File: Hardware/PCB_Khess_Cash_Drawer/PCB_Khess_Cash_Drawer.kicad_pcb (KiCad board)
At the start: 2 copper layers, 121 x 60.1 mm, 22 parts, among them J1 Screw_Terminal_01x02, J2 Conn_01x03, J3 RJ11_Connector, Q1 BUK9637-100E,118, U1 R-78B5.0-2.0

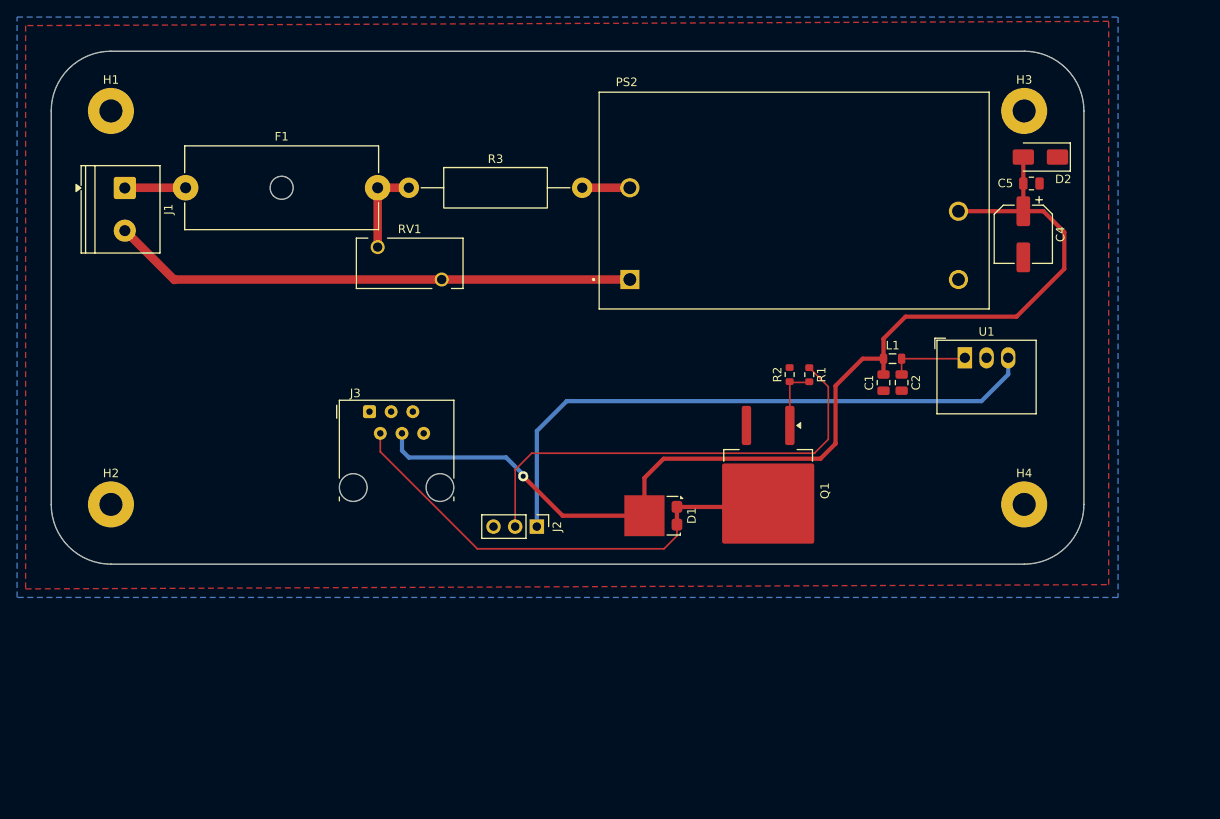
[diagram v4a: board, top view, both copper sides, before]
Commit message: fix: update pcb routing
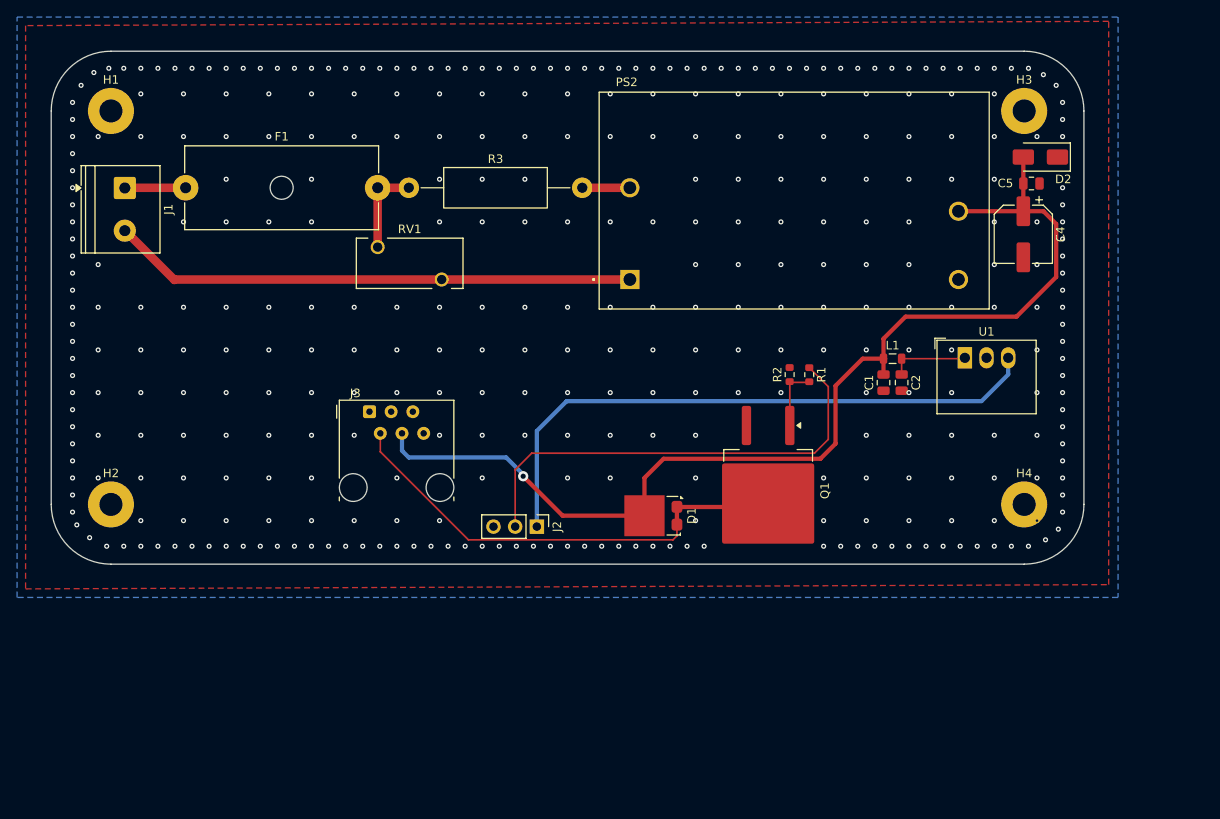
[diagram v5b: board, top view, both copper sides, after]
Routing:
- net CASH_DRAWER_DRIVE: track 56.5 -> 55.6 mm
- net +12V: track 131.9 -> 131.2 mm
- net GND: vias 0 -> 361

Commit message: feat: add gerbers
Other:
- board text added: "B"
- board text added: "B. ING N. KRIMAT M. LAPLANTE R. LAGHOUANE"
- board text added: "E. ZHANG C. JOURNEAU R. BOUCHIKHI"
- board text added: "T"
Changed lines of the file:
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@@
 			(outputformat 1)
 			(mirror no)
-			(drillshape 1)
+			(drillshape 0)
 			(scaleselection 1)
-			(outputdirectory "")
+			(outputdirectory "gerbers/")
 		)
 	)
@@
 		(layer "Edge.Cuts")
 	)
+	(gr_text "B. ING\nN. KRIMAT\nM. LAPLANTE\nR. LAGHOUANE"
+		(at 81.9 82.2 0)
+		(layer "F.Cu")
+		(effects
+			(font
+				(size 0.5 0.5)
+				(thickness 0.125)
+			)
+			(justify left bottom)
+		)
+	)
+	(gr_text "E. ZHANG\nC. JOURNEAU\nR. BOUCHIKHI"
+		(at 87.9 81.395028 0)
+		(layer "F.Cu")
+		(effects
+			(font
+				(size 0.5 0.5)
+				(thickness 0.125)
+			)
+			(justify left bottom)
+		)
+	)
+	(gr_text "T"
+		(at 85 86.5 0)
+		(layer "F.Cu")
+		(effects
+			(font
+				(size 1.5 1.5)
+				(thickness 0.3)
+				(bold yes)
+			)
+			(justify left bottom)
+		)
+	)
+	(gr_text "B"
+		(at 86.7 86.5 0)
+		(layer "B.Cu")
+		(effects
+			(font
+				(size 1.5 1.5)
+				(thickness 0.3)
+				(bold yes)
+			)
+			(justify left bottom mirror)
+		)
+	)
 	(via

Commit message: feat: case cash drawer with turbocase
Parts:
- added ?: , Cutout_Pinheader_01x03_254, F.Cu at (127.5, 92.3)
- added ?: , Cutout_Pinheader_01x02_254, F.Cu at (112.8, 92.2)
- added ?: , Cutout_Pinheader_02x04_254, F.Cu at (75.1, 51.6)
